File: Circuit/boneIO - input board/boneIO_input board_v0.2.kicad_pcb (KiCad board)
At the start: 2 copper layers, 231 x 74 mm, 175 parts, among them J1 I2C_OUT, J2 Screw_Terminal_01x08, J3 Screw_Terminal_01x08, J4 Screw_Terminal_01x08, J5 Screw_Terminal_01x08, J6 Screw_Terminal_01x08, J7 Screw_Terminal_01x08, J9 Conn_02x13_Odd_Even, P3 BeagleBone_Black_Header, P4 BeagleBone_Black_Header, SW1 SW_Push, U1 LM2596S-ADJ, U10 PC847, U11 PC847, U12 PC847, U13 DS1307Z+, U2 PC847, U3 PC847, U4 PC847, U5 PC847, U6 PC847, U7 PC847, U8 PC847, U9 PC847, Y1 32,788 MHz

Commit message: Zmiany 27-10-2021
nowa PCB
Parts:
- removed AN1: Screw_Terminal_01x07, Connector_Phoenix_MSTB:PhoenixContact_MSTBA_2,5_7-G_1x07_P5.00mm_Horizontal
- removed the C10 at (103.1, 84.3)
- removed the C17 at (73.5, 84.4)
- removed the C18 at (46.9, 85.3)
- removed the C9 at (43.1, 97.3)
- removed the J1 at (224.1, 117.7)
- removed the R15 at (45.6, 101.2)
- removed the R16 at (100.6, 81.0)
- removed the R17 at (73.6, 81.1)
- removed the R30 at (41.8, 81.8)
- removed the R36 at (39.2, 81.8)
- removed the R37 at (71.4, 100.9)
- removed the R42 at (38.1, 101.1)
- removed R51, R52, R53, R54, R55, R56, R57, R58, R59, R60, R61, R62, R63, R64, R65, R66, R67, R68, R69, R70, R71, R72, R73, R74, R75, R76, R77, R78, R79, R80, R81, R82, R83, R84, R85, R86, R87, R88, R89, R90, R91: 10k, Resistor_SMD:R_0603_1608Metric
- removed the U9 at (84.0, 107.6)
- added C31: 100n, Capacitor_SMD:C_0603_1608Metric, F.Cu at (220.9, 11.8)
- added C39: 100n, Capacitor_SMD:C_0603_1608Metric, F.Cu at (216.9, 5.49)
- added C43: 100n, Capacitor_SMD:C_0603_1608Metric, F.Cu at (204.3, 16.8)
- added C44: 100n, Capacitor_SMD:C_0603_1608Metric, F.Cu at (218.8, 1.72)
- added G***: LOGO, test, F.Cu at (0.00, 0.00)
- added G***: LOGO, Symbol:test2, F.Cu at (46.2, 89.2)
- added J7: Screw_Terminal_01x08, Connector:8pin, F.Cu at (251.7, 60.4)
- added J9: Screw_Terminal_01x08, Connector:8pin, F.Cu at (216.2, 121.2)
- added PS1: B2424S-1WR2, Module:CONV_B0505S-1WR2, F.Cu at (85.2, 90.2)
- added R39: 10k, Resistor_SMD:R_0603_1608Metric, F.Cu at (190.4, 33.7)
- added R45: 10k, Resistor_SMD:R_0603_1608Metric, F.Cu at (190.4, 36.2)
- added R46: 10k, Resistor_SMD:R_0603_1608Metric, F.Cu at (196.3, 26.8)
- added R47: 10k, Resistor_SMD:R_0603_1608Metric, F.Cu at (194.4, 31.9)
- added R48: 10k, Resistor_SMD:R_0603_1608Metric, F.Cu at (220.9, 6.74)
- added R49: 10k, Resistor_SMD:R_0603_1608Metric, F.Cu at (216.9, 10.5)
- added REF**: YAAJ_DCDC_StepDown_LM2596, Module:YAAJ_DCDC_StepDown_LM2596, F.Cu at (141.9, 82.4)
- added U1: EL357N-G, Package_SO:OPTO_EL357N-G, F.Cu at (97.2, 72.7)
- added U13: EL357N-G, Package_SO:OPTO_EL357N-G, F.Cu at (63.8, 72.7)
- added U14: EL357N-G, Package_SO:OPTO_EL357N-G, F.Cu at (125.2, 108.0)
- added U15: EL357N-G, Package_SO:OPTO_EL357N-G, F.Cu at (130.0, 108.0)
- added U16: EL357N-G, Package_SO:OPTO_EL357N-G, F.Cu at (59.1, 72.7)
- added U17: EL357N-G, Package_SO:OPTO_EL357N-G, F.Cu at (54.4, 72.8)
- added U18: EL357N-G, Package_SO:OPTO_EL357N-G, F.Cu at (49.6, 72.8)
- added U19: EL357N-G, Package_SO:OPTO_EL357N-G, F.Cu at (44.9, 72.7)
- added U20: EL357N-G, Package_SO:OPTO_EL357N-G, F.Cu at (40.1, 72.8)
- added U21: EL357N-G, Package_SO:OPTO_EL357N-G, F.Cu at (35.3, 72.7)
- added U22: EL357N-G, Package_SO:OPTO_EL357N-G, F.Cu at (130.3, 72.7)
- added U23: EL357N-G, Package_SO:OPTO_EL357N-G, F.Cu at (125.6, 72.7)
- added U24: EL357N-G, Package_SO:OPTO_EL357N-G, F.Cu at (120.8, 72.7)
- added U25: EL357N-G, Package_SO:OPTO_EL357N-G, F.Cu at (116.1, 72.7)
- added U26: EL357N-G, Package_SO:OPTO_EL357N-G, F.Cu at (111.3, 72.7)
- added U27: EL357N-G, Package_SO:OPTO_EL357N-G, F.Cu at (106.6, 72.7)
- added U28: RS485, Module:RS485_moduleTTL, B.Cu at (227.5, 67.0)
- added U29: EL357N-G, Package_SO:OPTO_EL357N-G, F.Cu at (101.9, 72.7)
- added U30: EL357N-G, Package_SO:OPTO_EL357N-G, F.Cu at (35.3, 108.0)
- added U31: EL357N-G, Package_SO:OPTO_EL357N-G, F.Cu at (40.0, 108.0)
- added U32: EL357N-G, Package_SO:OPTO_EL357N-G, F.Cu at (44.8, 108.0)
- added U34: EL357N-G, Package_SO:OPTO_EL357N-G, F.Cu at (49.5, 108.0)
- added U35: EL357N-G, Package_SO:OPTO_EL357N-G, F.Cu at (54.2, 108.0)
- added U36: EL357N-G, Package_SO:OPTO_EL357N-G, F.Cu at (58.9, 108.0)
- added U37: EL357N-G, Package_SO:OPTO_EL357N-G, F.Cu at (63.6, 108.0)
- added U38: EL357N-G, Package_SO:OPTO_EL357N-G, F.Cu at (68.3, 108.0)
- added U39: EL357N-G, Package_SO:OPTO_EL357N-G, F.Cu at (73.1, 108.0)
- added U40: EL357N-G, Package_SO:OPTO_EL357N-G, F.Cu at (77.8, 108.0)
- added U41: EL357N-G, Package_SO:OPTO_EL357N-G, F.Cu at (82.6, 108.0)
- added U42: EL357N-G, Package_SO:OPTO_EL357N-G, F.Cu at (87.3, 108.0)
- added U43: EL357N-G, Package_SO:OPTO_EL357N-G, F.Cu at (92.0, 108.0)
- added U44: EL357N-G, Package_SO:OPTO_EL357N-G, F.Cu at (96.8, 108.0)
- added U45: EL357N-G, Package_SO:OPTO_EL357N-G, F.Cu at (101.5, 108.0)
- BT1: footprint Battery:BatteryHolder_Keystone_103_1x20mm -> Battery:Battery_Panasonic_CR1220-VCN_Vertical_CircularHoles; moved to F.Cu
- R50: moved to F.Cu
- SW1: footprint Button_Switch_THT:SW_PUSH_6mm_H8mm -> Button_Switch_THT:SW_PUSH_6mm_H13mm
- U10, U11, U12, U2, U3, U4, U5, U6, U7, U8: value PC847 -> EL357N-G; footprint Package_SO:SOP-16_4.55x10.3mm_P1.27mm -> Package_SO:OPTO_EL357N-G
- Y1: footprint Crystal:Crystal_C38-LF_D3.0mm_L8.0mm_Horizontal_1EP_style1 -> Crystal:Crystal_C26-LF_D2.1mm_L6.5mm_Horizontal; moved to F.Cu
- moved R18 192.9 mm to (218.8, -5.81), turned to 0 degrees
- moved C41 185.9 mm to (222.8, -0.79), turned to 0 degrees
- moved R6 184.0 mm to (218.8, -3.30), turned to 0 degrees
- moved R21 183.2 mm to (208.9, 5.49), turned to 0 degrees
- moved C21 181.2 mm to (212.9, 13.0), turned to 0 degrees
- moved R41 180.2 mm to (220.9, 4.23), turned to 0 degrees
- moved C15 179.9 mm to (208.3, 20.6), turned to 0 degrees
- moved R3 179.5 mm to (200.3, 19.3), turned to 0 degrees
- moved C42 179.0 mm to (200.3, 21.8), turned to 0 degrees
- moved C36 174.3 mm to (204.3, 29.3), turned to 0 degrees
- moved C12 174.1 mm to (208.9, 8.00), turned to 0 degrees
- moved R33 173.7 mm to (208.9, 15.5), turned to 0 degrees
- moved C24 170.3 mm to (204.3, 26.8), turned to 0 degrees
- moved C7 168.6 mm to (218.8, -0.79), turned to 0 degrees
- moved C25 166.3 mm to (212.3, 18.0), turned to 0 degrees
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- renumbered C44 to C10, C47 to C17, C48 to C18, C43 to C9, D2 to D1, D3 to D2, D4 to D3, J3 to J1, J5 to J2, J4 to J3, J6 to J4, J2 to J5, J7 to J6, J9 to J8, L2 to L1, L1 to L2, P4 to P1, P3 to P2, R47 to R15, R48 to R16, R49 to R17, R45 to R30, R46 to R31, R94 to R36, R95 to R37, R96 to R42, U13 to U33, U1 to U9
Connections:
- net P9.32 renamed VDD_ADC
- net P9.34 renamed GND_ADC
- C1 pad 1: P8.18 -> Net-(C1-Pad1)
- C1 pad 2: GND -> P8.46_OUT
- C11 pad 1: P8.38 -> Net-(C11-Pad1)
- C11 pad 2: GND -> P8.42_OUT
- C12 pad 1: P8.31 -> Net-(C12-Pad1)
- C12 pad 2: GND -> P8.41_OUT
- C13 pad 1: P8.16 -> Net-(C13-Pad1)
- C13 pad 2: GND -> P8.40_OUT
- C14 pad 1: P8.09 -> Net-(C14-Pad1)
- C14 pad 2: GND -> P8.39_OUT
- C15 pad 1: P8.23 -> Net-(C15-Pad1)
- C15 pad 2: GND -> P8.04_OUT
- C16 pad 1: P8.44 -> Net-(C16-Pad1)
- C16 pad 2: GND -> P8.03_OUT
- C19 pad 1: P8.15 -> Net-(C19-Pad1)
- C19 pad 2: GND -> P8.38_OUT
- C2 pad 1: P8.11 -> Net-(C2-Pad1)
- C2 pad 2: GND -> P8.45_OUT
- C20 pad 1: P8.08 -> Net-(C20-Pad1)
- C20 pad 2: GND -> P8.37_OUT
- C21 pad 1: P8.22 -> Net-(C21-Pad1)
- C21 pad 2: GND -> P8.36_OUT
- C22 pad 1: P8.43 -> Net-(C22-Pad1)
- C22 pad 2: GND -> P8.35_OUT
- C23 pad 1: P8.36 -> Net-(C23-Pad1)
- C23 pad 2: GND -> P8.34_OUT
- C24 pad 1: P8.29 -> Net-(C24-Pad1)
- C24 pad 2: GND -> P8.33_OUT
- C25 pad 1: P8.14 -> Net-(C25-Pad1)
- C25 pad 2: GND -> P8.32_OUT
- C26 pad 1: P8.07 -> Net-(C26-Pad1)
- C26 pad 2: GND -> P8.31_OUT
- C27 pad 1: P8.21 -> Net-(C27-Pad1)
- C27 pad 2: GND -> P8.30_OUT
- C28 pad 1: P8.42 -> Net-(C28-Pad1)
- C28 pad 2: GND -> P8.29_OUT
- C29 pad 1: P8.35 -> Net-(C29-Pad1)
- C29 pad 2: GND -> P8.28_OUT
- C3 pad 1: P8.25 -> Net-(C3-Pad1)
- C3 pad 2: GND -> P8.44_OUT
- C30 pad 1: P8.28 -> Net-(C30-Pad1)
- C30 pad 2: GND -> P8.27_OUT
- C32 pad 1: P8.06 -> Net-(C32-Pad1)
- C32 pad 2: GND -> P8.25_OUT
- C33 pad 1: P8.20 -> Net-(C33-Pad1)
- C33 pad 2: GND -> P8.24_OUT
- C34 pad 1: P8.41 -> Net-(C34-Pad1)
- C34 pad 2: GND -> P8.23_OUT
- C35 pad 1: P8.34 -> Net-(C35-Pad1)
- C35 pad 2: GND -> P8.22_OUT
- C36 pad 1: P8.27 -> Net-(C36-Pad1)
- C36 pad 2: GND -> P8.21_OUT
- C37 pad 1: P8.12 -> Net-(C37-Pad1)
- C37 pad 2: GND -> P8.20_OUT
- C38 pad 1: P8.05 -> Net-(C38-Pad1)
- C38 pad 2: GND -> P8.18_OUT
- C4 pad 1: P8.46 -> Net-(C4-Pad1)
- C4 pad 2: GND -> P8.43_OUT
- C40 pad 1: P8.40 -> Net-(C40-Pad1)
- C40 pad 2: GND -> P8.16_OUT
- C41 pad 1: P8.33 -> Net-(C41-Pad1)
- C41 pad 2: GND -> P8.15_OUT
- C42 pad 1: P8.26 -> Net-(C42-Pad1)
- C42 pad 2: GND -> P8.14_OUT
- C45 pad 1: P8.04 -> Net-(C45-Pad1)
- C45 pad 2: GND -> P8.10_OUT
- C46 pad 1: P8.03 -> Net-(C46-Pad1)
- C46 pad 2: GND -> P8.09_OUT
- C5 pad 1: P8.39 -> Net-(C5-Pad1)
- C5 pad 2: GND -> P8.08_OUT
- C6 pad 1: P8.32 -> Net-(C6-Pad1)
- C6 pad 2: GND -> P8.07_OUT
- C7 pad 1: P8.17 -> Net-(C7-Pad1)
- C7 pad 2: GND -> P8.06_OUT
- C8 pad 1: P8.10 -> Net-(C8-Pad1)
- C8 pad 2: GND -> P8.05_OUT
- J1 pad 2: Net-(J3-Pad2) -> P8.46_OUT
- J1 pad 3: Net-(J3-Pad3) -> P8.45_OUT
- J1 pad 4: Net-(J3-Pad4) -> P8.44_OUT
- J1 pad 5: Net-(J3-Pad5) -> P8.43_OUT
- J1 pad 6: Net-(J3-Pad6) -> P8.42_OUT
- J1 pad 7: Net-(J3-Pad7) -> P8.41_OUT
- J1 pad 8: Net-(J3-Pad8) -> P8.40_OUT
- J2 pad 2: Net-(J5-Pad2) -> P8.25_OUT
- J2 pad 3: Net-(J5-Pad3) -> P8.24_OUT
- J2 pad 4: Net-(J5-Pad4) -> P8.23_OUT
- J2 pad 5: Net-(J5-Pad5) -> P8.22_OUT
- J2 pad 6: Net-(J5-Pad6) -> P8.21_OUT
- J2 pad 7: Net-(J5-Pad7) -> P8.20_OUT
- J2 pad 8: Net-(J5-Pad8) -> P8.18_OUT
- J3 pad 2: Net-(J4-Pad2) -> P8.39_OUT
- J3 pad 3: Net-(J4-Pad3) -> P8.38_OUT
- J3 pad 4: Net-(J4-Pad4) -> P8.37_OUT
- J3 pad 5: Net-(J4-Pad5) -> P8.36_OUT
- J3 pad 6: Net-(J4-Pad6) -> P8.35_OUT
- J3 pad 7: Net-(J4-Pad7) -> P8.34_OUT
- J3 pad 8: Net-(J4-Pad8) -> P8.33_OUT
- J4 pad 2: Net-(J6-Pad2) -> P8.17_OUT
- J4 pad 3: Net-(J6-Pad3) -> P8.16_OUT
- J4 pad 4: Net-(J6-Pad4) -> P8.15_OUT
- J4 pad 5: Net-(J6-Pad5) -> P8.14_OUT
- J4 pad 6: Net-(J6-Pad6) -> P8.12_OUT
- J4 pad 7: Net-(J6-Pad7) -> P8.11_OUT
- J4 pad 8: Net-(J6-Pad8) -> P8.10_OUT
- J5 pad 2: Net-(J2-Pad2) -> P8.32_OUT
- J5 pad 3: Net-(J2-Pad3) -> P8.31_OUT
- J5 pad 4: Net-(J2-Pad4) -> P8.30_OUT
- J5 pad 5: Net-(J2-Pad5) -> P8.29_OUT
- J5 pad 6: Net-(J2-Pad6) -> P8.28_OUT
- J5 pad 7: Net-(J2-Pad7) -> P8.27_OUT
- J5 pad 8: Net-(J2-Pad8) -> P8.26_OUT
- J6 pad 2: Net-(J7-Pad2) -> P8.09_OUT
- J6 pad 3: Net-(J7-Pad3) -> P8.08_OUT
- J6 pad 4: Net-(J7-Pad4) -> P8.07_OUT
- J6 pad 5: Net-(J7-Pad5) -> P8.06_OUT
- J6 pad 6: Net-(J7-Pad6) -> P8.05_OUT
- J6 pad 7: Net-(J7-Pad7) -> P8.04_OUT
- J6 pad 8: Net-(J7-Pad8) -> P8.03_OUT
- J8 pad 16: P9.26 -> P8.19
- J8 pad 20: P9.24 -> P8.13
- R1 pad 1: +3V3 -> Net-(C1-Pad1)
- R1 pad 2: P8.18 -> +24VA
- R10 pad 1: +3V3 -> Net-(C12-Pad1)
- R10 pad 2: P8.45 -> +24VA
- R11 pad 1: +3V3 -> Net-(C13-Pad1)
- R11 pad 2: P8.38 -> +24VA
- R12 pad 1: +3V3 -> Net-(C14-Pad1)
- R12 pad 2: P8.31 -> +24VA
- R13 pad 1: +3V3 -> Net-(C15-Pad1)
- R13 pad 2: P8.16 -> +24VA
- R14 pad 1: +3V3 -> Net-(C16-Pad1)
- R14 pad 2: P8.09 -> +24VA
- R18 pad 1: +3V3 -> Net-(C19-Pad1)
- R18 pad 2: P8.30 -> +24VA
- R19 pad 1: +3V3 -> Net-(C20-Pad1)
- R19 pad 2: P8.15 -> +24VA
- R2 pad 1: +3V3 -> Net-(C2-Pad1)
- R2 pad 2: P8.11 -> +24VA
- R20 pad 1: +3V3 -> Net-(C21-Pad1)
- R20 pad 2: P8.08 -> +24VA
- R21 pad 1: +3V3 -> Net-(C22-Pad1)
- R21 pad 2: P8.22 -> +24VA
- R22 pad 1: +3V3 -> Net-(C23-Pad1)
- R22 pad 2: P8.43 -> +24VA
- R23 pad 1: +3V3 -> Net-(C24-Pad1)
- R23 pad 2: P8.36 -> +24VA
- R24 pad 1: +3V3 -> Net-(C25-Pad1)
- R24 pad 2: P8.29 -> +24VA
- R25 pad 1: +3V3 -> Net-(C26-Pad1)
- R25 pad 2: P8.14 -> +24VA
- R26 pad 1: +3V3 -> Net-(C27-Pad1)
- R26 pad 2: P8.07 -> +24VA
- R27 pad 1: +3V3 -> Net-(C28-Pad1)
- R27 pad 2: P8.21 -> +24VA
- R28 pad 1: +3V3 -> Net-(C29-Pad1)
- R28 pad 2: P8.42 -> +24VA
- R29 pad 1: +3V3 -> Net-(C30-Pad1)
- R29 pad 2: P8.35 -> +24VA
- R3 pad 1: +3V3 -> Net-(C3-Pad1)
- R3 pad 2: P8.25 -> +24VA
- R32 pad 1: +3V3 -> Net-(C31-Pad1)
- R32 pad 2: P8.06 -> +24VA
- R33 pad 1: +3V3 -> Net-(C32-Pad1)
- R33 pad 2: P8.20 -> +24VA
- R34 pad 1: +3V3 -> Net-(C33-Pad1)
- R34 pad 2: P8.41 -> +24VA
- R35 pad 1: +3V3 -> Net-(C34-Pad1)
- R35 pad 2: P8.34 -> +24VA
- R38 pad 1: +3V3 -> Net-(C35-Pad1)
- R38 pad 2: P8.05 -> +24VA
- R4 pad 1: +3V3 -> Net-(C4-Pad1)
- R4 pad 2: P8.46 -> +24VA
- R40 pad 1: +3V3 -> Net-(C37-Pad1)
- R40 pad 2: P8.40 -> +24VA
- R41 pad 1: +3V3 -> Net-(C38-Pad1)
- R41 pad 2: P8.33 -> +24VA
- R43 pad 1: +3V3 -> Net-(C39-Pad1)
- R43 pad 2: P8.04 -> +24VA
- R44 pad 1: +3V3 -> Net-(C40-Pad1)
- R44 pad 2: P8.03 -> +24VA
- R5 pad 1: +3V3 -> Net-(C5-Pad1)
- R5 pad 2: P8.39 -> +24VA
- R50 pad 1: +24V -> Net-(C46-Pad1)
- R50 pad 2: Net-(R50-Pad2) -> +24VA
- R6 pad 1: +3V3 -> Net-(C6-Pad1)
- R6 pad 2: P8.32 -> +24VA
- R7 pad 1: +3V3 -> Net-(C7-Pad1)
- R7 pad 2: P8.17 -> +24VA
- R8 pad 1: +3V3 -> Net-(C8-Pad1)
- R8 pad 2: P8.10 -> +24VA
- R9 pad 1: +3V3 -> Net-(C11-Pad1)
- R9 pad 2: P8.24 -> +24VA
- U10 pad 1: Net-(R82-Pad2) -> Net-(C11-Pad1)
- U10 pad 2: Net-(J6-Pad6) -> P8.42_OUT
- U10 pad 3: Net-(R83-Pad2) -> GND
- U10 pad 4: Net-(J6-Pad7) -> P8.42
- U11 pad 1: Net-(R86-Pad2) -> Net-(C12-Pad1)
- U11 pad 2: Net-(J7-Pad3) -> P8.41_OUT
- U11 pad 3: Net-(R87-Pad2) -> GND
- U11 pad 4: Net-(J7-Pad4) -> P8.41
- U12 pad 1: Net-(R90-Pad2) -> Net-(C13-Pad1)
- U12 pad 2: Net-(J7-Pad7) -> P8.40_OUT
- U12 pad 3: Net-(R91-Pad2) -> GND
- U12 pad 4: Net-(J7-Pad8) -> P8.40
- U2 pad 1: Net-(R50-Pad2) -> Net-(C2-Pad1)
- U2 pad 2: Net-(J2-Pad2) -> P8.45_OUT
- U2 pad 3: Net-(R51-Pad2) -> GND
- U2 pad 4: Net-(J2-Pad3) -> P8.45
- U3 pad 1: Net-(R54-Pad2) -> Net-(C3-Pad1)
- U3 pad 2: Net-(J2-Pad6) -> P8.44_OUT
- U3 pad 3: Net-(R55-Pad2) -> GND
- U3 pad 4: Net-(J2-Pad7) -> P8.44
- U4 pad 1: Net-(R58-Pad2) -> Net-(C4-Pad1)
- U4 pad 2: Net-(J3-Pad3) -> P8.43_OUT
- U4 pad 3: Net-(R59-Pad2) -> GND
- U4 pad 4: Net-(J3-Pad4) -> P8.43
- U5 pad 1: Net-(R62-Pad2) -> Net-(C5-Pad1)
- U5 pad 2: Net-(J3-Pad7) -> P8.08_OUT
- U5 pad 3: Net-(R63-Pad2) -> GND
- U5 pad 4: Net-(J3-Pad8) -> P8.08
- U6 pad 1: Net-(R66-Pad2) -> Net-(C6-Pad1)
- U6 pad 2: Net-(J4-Pad4) -> P8.07_OUT
- U6 pad 3: Net-(R67-Pad2) -> GND
- U6 pad 4: Net-(J4-Pad5) -> P8.07
- U7 pad 1: Net-(R70-Pad2) -> Net-(C7-Pad1)
- U7 pad 2: Net-(J4-Pad8) -> P8.06_OUT
- U7 pad 3: Net-(R71-Pad2) -> GND
- U7 pad 4: Net-(J5-Pad2) -> P8.06
- U8 pad 1: Net-(R74-Pad2) -> Net-(C8-Pad1)
- U8 pad 2: Net-(J5-Pad5) -> P8.05_OUT
- U8 pad 3: Net-(R75-Pad2) -> GND
- U8 pad 4: Net-(J5-Pad6) -> P8.05
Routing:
- net P8.42: track 126.4 -> 0.00 mm, vias 1 -> 0
- net P8.43: track 122.7 -> 0.00 mm, vias 1 -> 0
- net P8.45: track 118.2 -> 0.00 mm, vias 1 -> 0
- net P8.44: track 117.5 -> 0.00 mm, vias 1 -> 0
- net P8.46: track 112.6 -> 0.00 mm, vias 1 -> 0
- net Earth: vias 118 -> 112
- net P8.30: vias 0 -> 2
- net Net-(BT1-Pad1): vias 0 -> 2
- net GND: vias 0 -> 2
- added copper zone on F.Cu, net +24V
- removed copper zone on F.Cu, net (none)
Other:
- board text added: "A+"
- board text added: "B-"
- board text added: "GND_RS"
- board text added: "LM2596"
- board text added: "RS485"
- board text added: "RTC CLOCK"
- board text added: "input board v0.2 Author - Kamil Bożyk"
- board text removed: "boneIO - input board v0.1 Author - Maciej Krasuski"

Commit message: Aktualizacja 28_10_2021
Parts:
- removed G***: LOGO, test
- removed G***: LOGO, Symbol:test2
- moved C32 204.8 mm to (35.7, 111.0)
- moved R33 199.1 mm to (35.8, 113.8)
- moved R41 191.3 mm to (64.1, 113.8)
- moved C34 190.0 mm to (45.2, 111.0)
- moved R35 183.8 mm to (45.2, 113.8)
- moved R34 183.2 mm to (40.5, 113.8)
- moved C41 182.8 mm to (78.2, 111.0)
- moved C39 181.9 mm to (68.8, 111.0)
- moved C22 181.7 mm to (44.3, 70.0), turned to 180 degrees
- moved R18 176.2 mm to (58.5, 67.2), turned to 180 degrees
- moved R21 175.8 mm to (44.3, 67.3), turned to 180 degrees
- moved C24 174.9 mm to (34.8, 70.0), turned to 180 degrees
- moved C21 173.5 mm to (49.1, 70.0), turned to 180 degrees
- moved C45 171.5 mm to (97.2, 111.0)
- moved C36 170.5 mm to (54.6, 111.0)
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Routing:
- net +24VA: track 0.00 -> 246.1 mm, vias 0 -> 42
- net P8.25: track 0.00 -> 195.1 mm, vias 0 -> 1
- net P8.24: track 0.00 -> 186.7 mm, vias 0 -> 1
- net P8.23: track 0.00 -> 184.5 mm, vias 0 -> 1
- net P8.22: track 0.00 -> 176.1 mm, vias 0 -> 1
- net P8.21: track 0.00 -> 173.3 mm, vias 0 -> 1
- net P8.20: track 0.00 -> 164.2 mm, vias 0 -> 1
- net P8.18: track 0.00 -> 156.9 mm, vias 0 -> 1
- net P8.17: track 0.00 -> 153.8 mm, vias 0 -> 1
- net P8.16: track 0.00 -> 144.6 mm, vias 0 -> 1
- net P8.15: track 0.00 -> 141.5 mm, vias 0 -> 1
- net P8.14: track 0.00 -> 133.1 mm, vias 0 -> 1
- net P8.12: track 0.00 -> 128.4 mm, vias 0 -> 1
- net P8.11: track 0.00 -> 126.4 mm, vias 0 -> 1
- net P8.10: track 0.00 -> 118.5 mm, vias 0 -> 1
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- added copper zone on B.Cu, net Earth
- added copper zone on F.Cu, net Earth
- added copper zone on B.Cu, net GNDA
- added copper zone on F.Cu, net GNDA
- removed copper zone on B.Cu, net GND

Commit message: Zmiany 28.10.2021_2
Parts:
- removed P1, P2: BeagleBone_Black_Header, Connector_PinHeader_2.54mm:PinHeader_2x23_P2.54mm_Vertical
- added C47: 100n, Capacitor_SMD:C_0603_1608Metric, F.Cu at (237.8, 85.2)
- added D4: BAT54A, Package_TO_SOT_SMD:SOT-23, F.Cu at (248.5, 78.5)
- added G***: LOGO, Symbol:boneIO_LOGO, F.Cu at (54.5, 87.0)
- added J10: BeagleBone_Black_Header, Connector_PinHeader_2.54mm:PinHeader_2x23_P2.54mm_Vertical, F.Cu at (259.5, 116.8)
- added J11: BeagleBone_Black_Header, Connector_PinHeader_2.54mm:PinHeader_2x23_P2.54mm_Vertical, F.Cu at (211.2, 116.8)
- added R51: 680R, Resistor_SMD:R_0603_1608Metric, F.Cu at (248.2, 82.0)
- added R52: 680R, Resistor_SMD:R_0603_1608Metric, F.Cu at (241.8, 85.2)
- added U46: P82B96, Package_SO:SO-8_3.9x4.9mm_P1.27mm, F.Cu at (239.3, 78.2)
- C9: value 100u/50V -> 100uF/50V
- D2: value 1N5825 -> SS34
- D3: value LED_GREEN -> LED_RED
- L1: value 4,7uH -> 4.7uH
- moved R24 66.2 mm to (63.6, 67.9)
- moved U22 66.2 mm to (63.7, 76.2)
- moved C25 66.2 mm to (63.6, 70.7)
- moved C26 66.1 mm to (58.9, 70.7)
- moved C27 66.1 mm to (54.2, 70.7)
- moved C28 66.1 mm to (49.4, 70.7)
- moved C29 66.1 mm to (44.7, 70.7)
- moved C30 66.1 mm to (40.0, 70.7)
- moved C31 66.1 mm to (35.2, 70.7)
- moved R25 66.1 mm to (58.9, 67.9)
- moved R26 66.1 mm to (54.1, 68.0)
- moved R27 66.1 mm to (49.4, 68.0)
- moved R28 66.1 mm to (44.7, 68.0)
- moved R29 66.1 mm to (40.0, 68.0)
- moved R32 66.1 mm to (35.2, 68.0)
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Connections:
- J1 pad 2: P8.46_OUT -> P8.39_OUT
- J1 pad 3: P8.45_OUT -> P8.38_OUT
- J1 pad 4: P8.44_OUT -> P8.37_OUT
- J1 pad 5: P8.43_OUT -> P8.36_OUT
- J1 pad 6: P8.42_OUT -> P8.35_OUT
- J1 pad 7: P8.41_OUT -> P8.34_OUT
- J1 pad 8: P8.40_OUT -> P8.33_OUT
- J3 pad 2: P8.39_OUT -> P8.32_OUT
- J3 pad 3: P8.38_OUT -> P8.31_OUT
- J3 pad 4: P8.37_OUT -> P8.30_OUT
- J3 pad 5: P8.36_OUT -> P8.29_OUT
- J3 pad 6: P8.35_OUT -> P8.28_OUT
- J3 pad 7: P8.34_OUT -> P8.27_OUT
- J3 pad 8: P8.33_OUT -> P8.26_OUT
- J5 pad 2: P8.32_OUT -> P8.46_OUT
- J5 pad 3: P8.31_OUT -> P8.45_OUT
- J5 pad 4: P8.30_OUT -> P8.44_OUT
- J5 pad 5: P8.29_OUT -> P8.43_OUT
- J5 pad 6: P8.28_OUT -> P8.42_OUT
- J5 pad 7: P8.27_OUT -> P8.41_OUT
- J5 pad 8: P8.26_OUT -> P8.40_OUT
- J9 pad 4: SCL -> SDA_OUT
- J9 pad 5: SDA -> SCL_OUT
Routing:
- net P9.11: track 0.00 -> 212.7 mm, vias 0 -> 1
- net P9.13: track 0.00 -> 207.3 mm, vias 0 -> 1
- net P9.12: track 0.00 -> 206.4 mm, vias 0 -> 1
- net P9.14: track 0.00 -> 201.0 mm, vias 0 -> 1
- net P9.15: track 0.00 -> 200.6 mm, vias 0 -> 1
- net P9.16: track 0.00 -> 194.3 mm, vias 0 -> 1
- net P8.26: track 0.00 -> 183.2 mm, vias 0 -> 1
- net P8.27: track 0.00 -> 180.9 mm, vias 0 -> 1
- net P8.28: track 0.00 -> 172.5 mm, vias 0 -> 1
- net P9.31: track 0.00 -> 171.3 mm, vias 0 -> 1
- net P8.29: track 0.00 -> 170.1 mm, vias 0 -> 1
- net P9.29: track 0.00 -> 166.4 mm, vias 0 -> 1
- net P9.30: track 0.00 -> 166.1 mm, vias 0 -> 1
- net P8.30: track 0.00 -> 161.7 mm, vias 0 -> 1
- net P9.27: track 0.00 -> 161.0 mm, vias 0 -> 1
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- added copper zone on B.Cu, net GND
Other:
- board text added: "1.Dołożyć Drganie styków na Switch 2. Poprawić poligony GND"
- board text added: "input board v0.2"
- board text removed: "input board v0.2 Author - Kamil Bożyk"

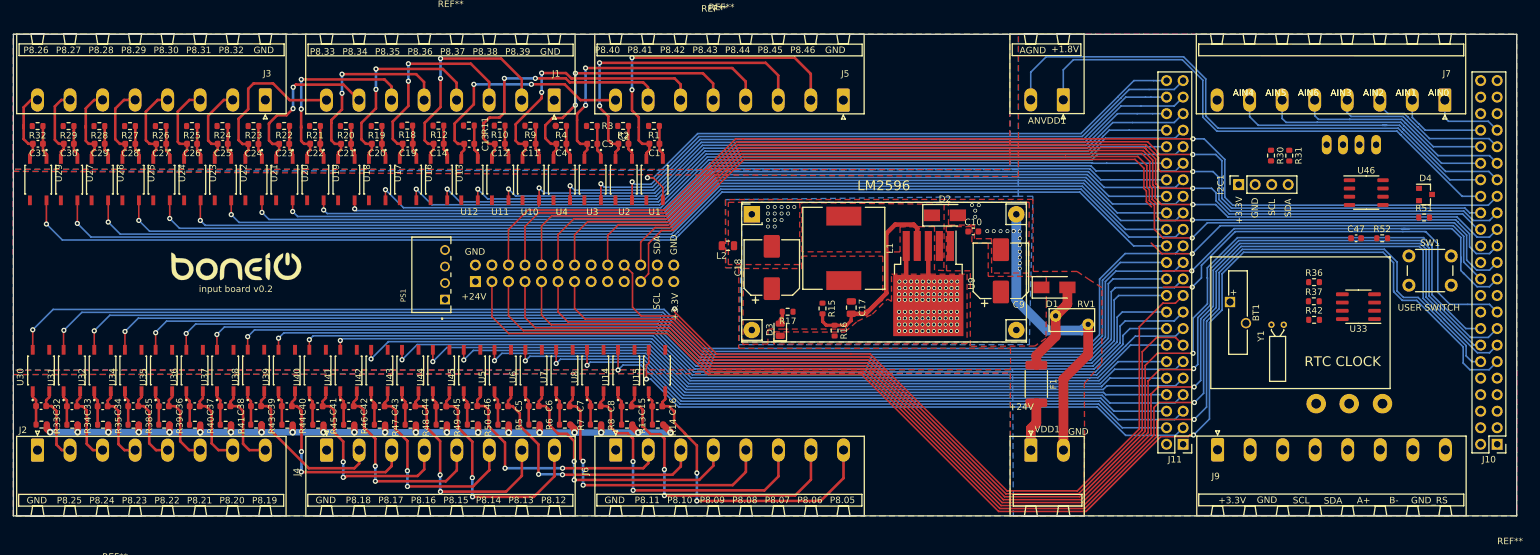
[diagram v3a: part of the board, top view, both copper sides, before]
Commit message: Input Board_v0.2_F
PCB ukończone do sprawdzenia.
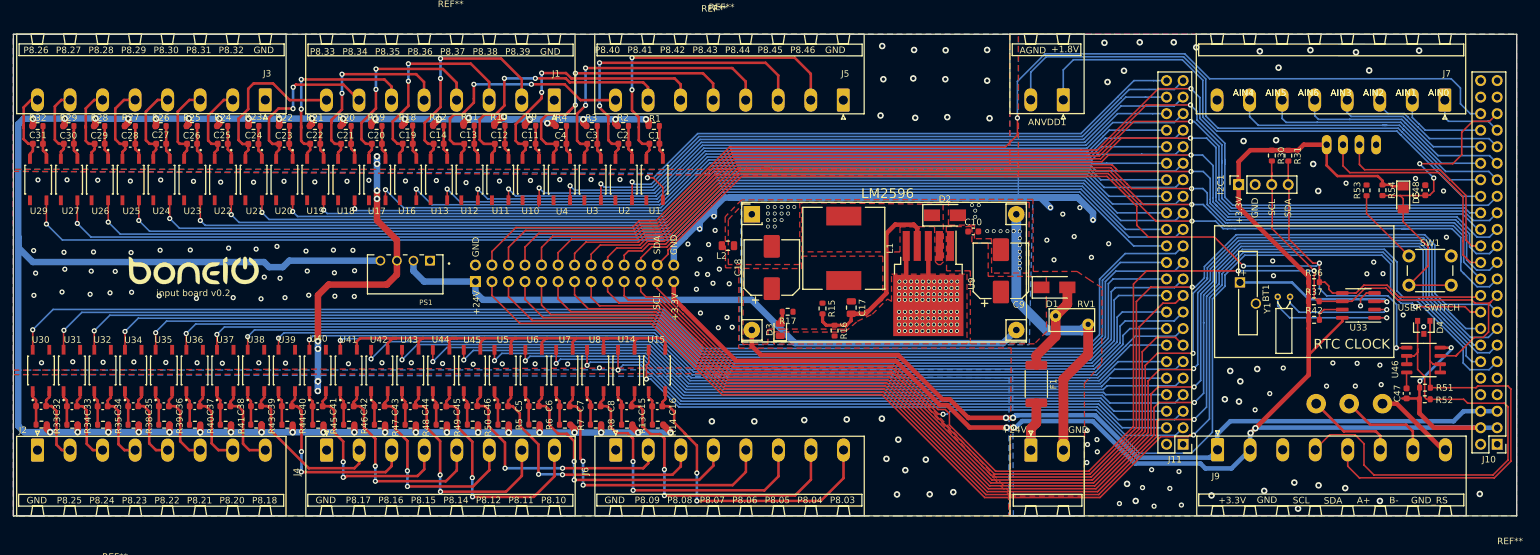
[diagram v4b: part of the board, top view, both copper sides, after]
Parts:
- added C48: 100n, Capacitor_SMD:C_0603_1608Metric, F.Cu at (248.4, 77.8)
- added D5: 1N4148, Diode_SMD:D_MiniMELF, F.Cu at (245.0, 79.0)
- added R53: 330R, Resistor_SMD:R_0603_1608Metric, F.Cu at (239.4, 77.8)
- added R54: 4.7k, Resistor_SMD:R_0603_1608Metric, F.Cu at (241.8, 77.8)
- moved U46 27.2 mm to (248.2, 103.9)
- moved R51 26.2 mm to (248.4, 108.2)
- moved R52 25.6 mm to (248.3, 109.9)
- moved C47 25.1 mm to (245.6, 109.0), turned to 90 degrees
- moved D4 20.4 mm to (248.2, 98.9), turned to 270 degrees
- moved G*** 6.55 mm to (48.0, 87.6)
- moved Y1 4.40 mm to (225.8, 94.2)
- moved PS1 4.02 mm to (91.7, 90.7), turned to 180 degrees
- moved BT1 3.37 mm to (219.9, 92.0)
- moved U33 0.20 mm to (238.2, 95.5)
- moved R31 0.15 mm to (227.4, 72.5)
- moved R30 0.13 mm to (224.8, 72.5)
- renumbered VDD1 to +24V
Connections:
- J8 pad 15: P9.17 -> P8.13
- J8 pad 16: P8.19 -> P9.25
- J8 pad 17: P9.18 -> P8.19
- J8 pad 18: P9.25 -> P9.23
- J8 pad 19: P9.21 -> P9.17
- J8 pad 20: P8.13 -> P9.22
- J8 pad 21: P9.22 -> P9.18
- J8 pad 22: P9.23 -> P9.21
- SW1 pad 1: GND -> Net-(R53-Pad1)
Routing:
- net +3V3: track 0.00 -> 261.5 mm, vias 0 -> 6
- net +24VA: track 121.4 -> 360.3 mm, vias 21 -> 42
- net SCL: track 0.00 -> 209.0 mm, vias 0 -> 2
- net GND: track 0.00 -> 207.2 mm, vias 0 -> 161
- net SDA: track 0.00 -> 188.8 mm, vias 0 -> 3
- net P9.42: track 0.00 -> 176.6 mm, vias 0 -> 1
- net P9.18: track 0.00 -> 173.3 mm, vias 0 -> 2
- net +5V: track 0.00 -> 130.0 mm, vias 0 -> 2
- net P9.17: track 65.4 -> 184.7 mm
- net +24V: track 0.00 -> 100.6 mm
- net P9.21: track 63.4 -> 151.2 mm
- net SDA_OUT: track 0.00 -> 73.5 mm
- net SCL_OUT: track 0.00 -> 67.5 mm
- net P9.41: track 0.00 -> 53.6 mm, vias 0 -> 2
- net GNDA: track 0.00 -> 47.6 mm, vias 0 -> 32
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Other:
- board text added: "P8.03"
- board text added: "P8.04"
- board text removed: "P8.13"
- board text removed: "P8.19"

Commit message: aktualizacja
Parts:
- removed J8: Conn_02x13_Odd_Even, Connector_PinSocket_2.54mm:PinSocket_2x13_P2.54mm_Vertical
- added J12: Conn_02x04_Odd_Even, Connector_PinHeader_2.54mm:PinHeader_2x04_P2.54mm_Vertical, B.Cu at (102.5, 89.3)
- renumbered +24V to VDD1
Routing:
- net P9.42: track 176.6 -> 151.4 mm
- net P9.31: track 180.2 -> 157.2 mm
- net P9.30: track 171.4 -> 150.9 mm
- net P9.11: track 209.1 -> 200.8 mm
- net P9.12: track 202.9 -> 195.4 mm
- net P9.13: track 204.0 -> 197.3 mm
- net P9.29: track 169.9 -> 164.7 mm
- net P9.14: track 198.4 -> 194.8 mm
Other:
- board text added: "+5V"
